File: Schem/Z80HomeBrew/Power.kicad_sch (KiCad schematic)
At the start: 23 parts, among them J1 PJ-037A, Q1 AO3401A, SW1 SW_Push, U1 AMS1117-3.3, U2 LTC2954CTS8-2_TRMPBF

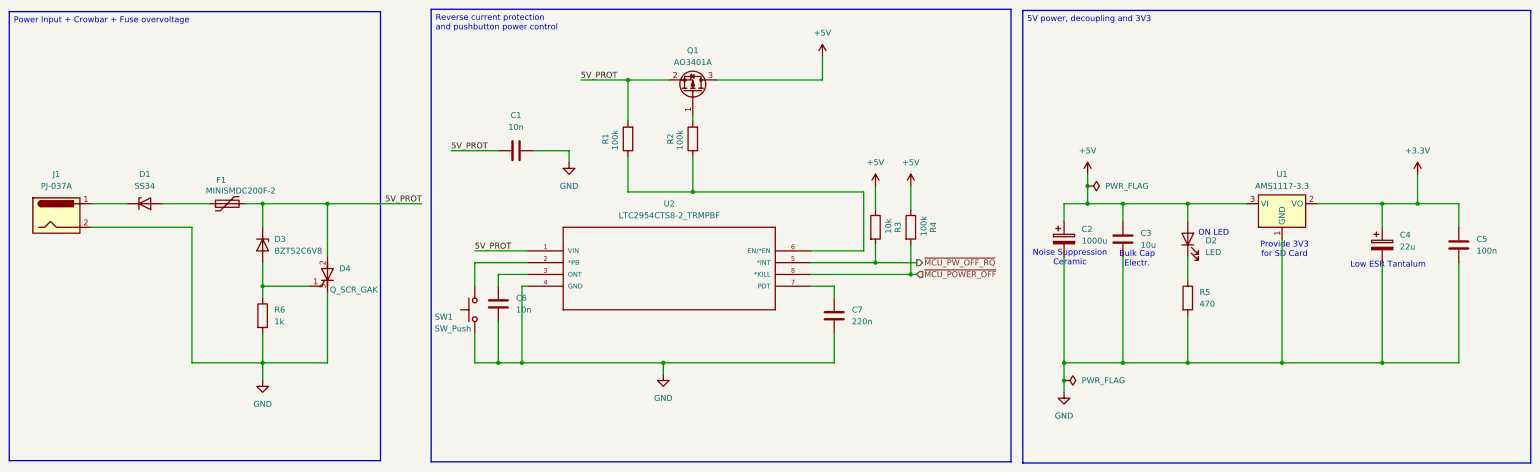
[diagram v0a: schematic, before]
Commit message: Added CPU, Address Decoding, Clock Tree, Console Port, SD Card, USB Ports schematics and associated symbols and footprints.
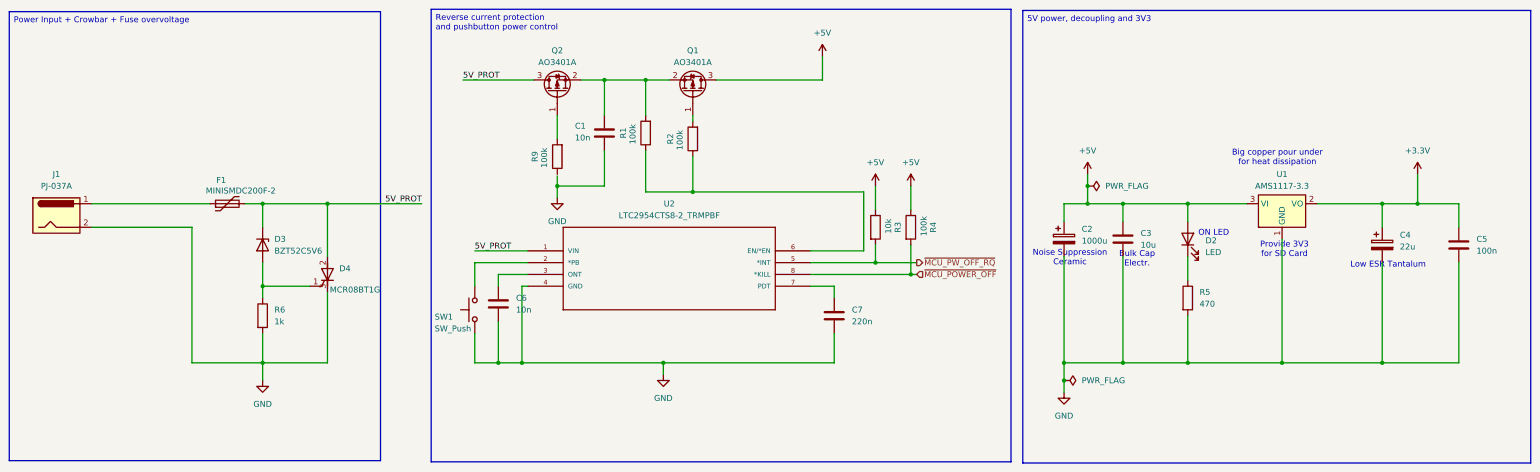
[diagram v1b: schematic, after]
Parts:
- removed D1: SS34, Diode_SMD:D_SMB-SMC_Universal_Handsoldering, symbol Device:D_Zener
- added Q2: AO3401A, Package_TO_SOT_SMD:SOT-23, symbol Transistor_FET:AO3401A
- added R9: 100k, Resistor_SMD:R_0603_1608Metric, symbol Device:R
- D3: value BZT52C6V8 -> BZT52C5V6
- D4: value Q_SCR_GAK -> MCR08BT1G
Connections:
- net 5V_PROT: now also Q2.3 (D); no longer C1.1, Q1.2 (S), R1.2
- net at F1.1: now also J1.1
- new net: C1.1, Q1.2 (S), Q2.2 (S), R1.2
- new net: Q2.1 (G), R9.2
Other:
- note added: "Big copper pour under for heat dissipation"
- moved on the sheet: R1

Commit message: Video block added. fixed some issues with parts...
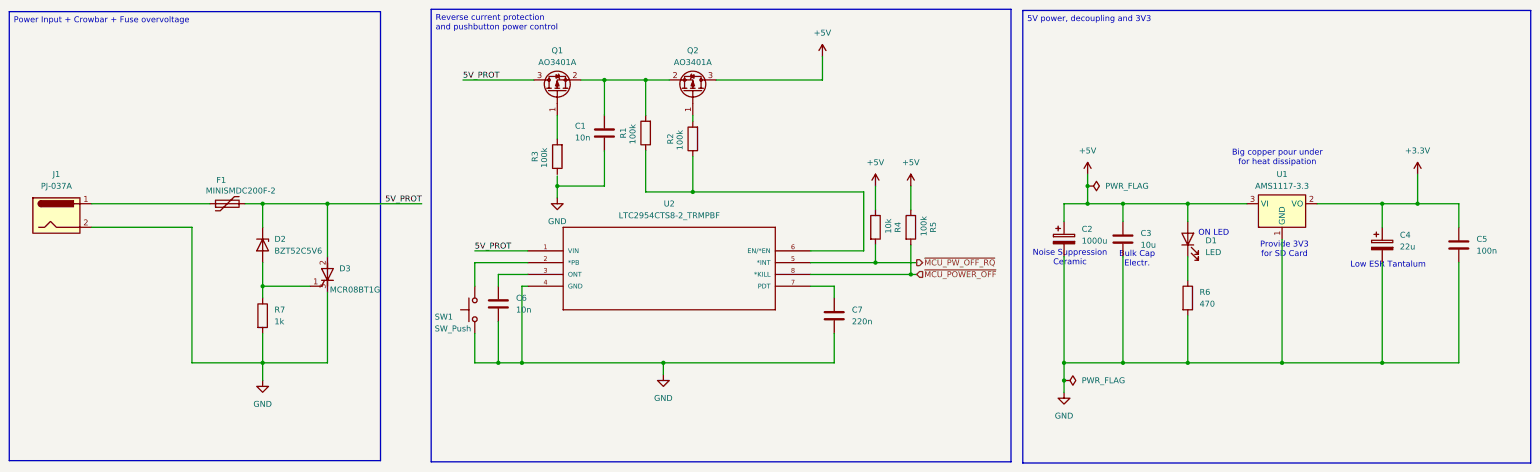
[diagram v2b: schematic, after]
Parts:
- renumbered D2 to D1, D3 to D2, D4 to D3, Q2 to Q1, Q1 to Q2, R9 to R3, R3 to R4, R4 to R5, R5 to R6, R6 to R7
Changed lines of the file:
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@@
 		(on_board yes)
 		(dnp no)
-		(property "Reference" "R4"
+		(property "Reference" "R5"
 			(at 229.616 76.2 90)
 			(effects
@@
 			(project "Z80HomeBrew"
 				(path "/5593e793-d133-45d0-a91e-72805049e474/3988d86f-c93e-49bc-9714-528a8b658c82"
-					(reference "R4")
+					(reference "R5")
 					(unit 1)
 				)
@@
 		(dnp no)
 		(fields_autoplaced yes)
-		(property "Reference" "#PWR05"
+		(property "Reference" "#PWR04"
 			(at 217.17 71.12 0)
 			(effects
@@
 			(project "Z80HomeBrew"
 				(path "/5593e793-d133-45d0-a91e-72805049e474/3988d86f-c93e-49bc-9714-528a8b658c82"
-					(reference "#PWR05")
+					(reference "#PWR04")
 					(unit 1)
 				)
@@
 		(on_board yes)
 		(dnp no)
-		(property "Reference" "R3"
+		(property "Reference" "R4"
 			(at 221.996 76.2 90)
 			(effects
@@
 			(project "Z80HomeBrew"
 				(path "/5593e793-d133-45d0-a91e-72805049e474/3988d86f-c93e-49bc-9714-528a8b658c82"
-					(reference "R3")
+					(reference "R4")
 					(unit 1)
 				)
@@
 		(on_board yes)
 		(dnp no)
-		(property "Reference" "Q2"
+		(property "Reference" "Q1"
 			(at 148.59 38.1 90)
 			(effects
@@
 			(project "Z80HomeBrew"
 				(path "/5593e793-d133-45d0-a91e-72805049e474/3988d86f-c93e-49bc-9714-528a8b658c82"
-					(reference "Q2")
+					(reference "Q1")
 					(unit 1)
 				)
@@
 		(dnp no)
 		(fields_autoplaced yes)
-		(property "Reference" "#PWR03"
+		(property "Reference" "#PWR02"
 			(at 262.89 68.58 0)
 			(effects
@@
 			(project ""
 				(path "/5593e793-d133-45d0-a91e-72805049e474/3988d86f-c93e-49bc-9714-528a8b658c82"
-					(reference "#PWR03")
+					(reference "#PWR02")
 					(unit 1)
 				)
@@
 		(on_board yes)
 		(dnp no)
-		(property "Reference" "R9"
+		(property "Reference" "R3"
 			(at 143.764 60.96 90)
 			(effects
@@
 			(project "Z80HomeBrew"
 				(path "/5593e793-d133-45d0-a91e-72805049e474/3988d86f-c93e-49bc-9714-528a8b658c82"
-					(reference "R9")
+					(reference "R3")
 					(unit 1)
 				)
@@
 		(dnp no)
 		(fields_autoplaced yes)
-		(property "Reference" "R6"
+		(property "Reference" "R7"
 			(at 87.63 93.9799 0)
 			(effects
@@
 			(project "Z80HomeBrew"
 				(path "/5593e793-d133-45d0-a91e-72805049e474/3988d86f-c93e-49bc-9714-528a8b658c82"
-					(reference "R6")
+					(reference "R7")
 					(unit 1)
 				)
@@
 		(dnp no)
 		(fields_autoplaced yes)
-		(property "Reference" "#PWR06"
+		(property "Reference" "#PWR05"
 			(at 224.79 71.12 0)
 			(effects
@@
 			(project "Z80HomeBrew"
 				(path "/5593e793-d133-45d0-a91e-72805049e474/3988d86f-c93e-49bc-9714-528a8b658c82"
-					(reference "#PWR06")
+					(reference "#PWR05")
 					(unit 1)
 				)
@@
 		(on_board yes)
 		(dnp no)
-		(property "Reference" "Q1"
+		(property "Reference" "Q2"
 			(at 177.8 38.1 90)
 			(effects
@@
 			(project ""
 				(path "/5593e793-d133-45d0-a91e-72805049e474/3988d86f-c93e-49bc-9714-528a8b658c82"
-					(reference "Q1")
+					(reference "Q2")
 					(unit 1)
 				)
@@
 		(on_board yes)
 		(dnp no)
-		(property "Reference" "D3"
+		(property "Reference" "D2"
 			(at 87.63 78.7399 90)
 			(effects
@@
 			(project ""
 				(path "/5593e793-d133-45d0-a91e-72805049e474/3988d86f-c93e-49bc-9714-528a8b658c82"
-					(reference "D3")
+					(reference "D2")
 					(unit 1)
 				)
@@
 		(dnp no)
 		(fields_autoplaced yes)
-		(property "Reference" "R5"
+		(property "Reference" "R6"
 			(at 287.02 90.1699 0)
 			(effects
@@
 			(project ""
 				(path "/5593e793-d133-45d0-a91e-72805049e474/3988d86f-c93e-49bc-9714-528a8b658c82"
-					(reference "R5")
+					(reference "R6")
 					(unit 1)
 				)
@@
 		(dnp no)
 		(fields_autoplaced yes)
-		(property "Reference" "#PWR020"
+		(property "Reference" "#PWR06"
 			(at 148.59 76.2 0)
 			(effects
@@
 			(project "Z80HomeBrew"
 				(path "/5593e793-d133-45d0-a91e-72805049e474/3988d86f-c93e-49bc-9714-528a8b658c82"
-					(reference "#PWR020")
+					(reference "#PWR06")
 					(unit 1)
 				)
@@
 		(dnp no)
 		(fields_autoplaced yes)
-		(property "Reference" "#PWR04"
+		(property "Reference" "#PWR03"
 			(at 334.01 68.58 0)
 			(effects
@@
 			(project ""
 				(path "/5593e793-d133-45d0-a91e-72805049e474/3988d86f-c93e-49bc-9714-528a8b658c82"
-					(reference "#PWR04")
+					(reference "#PWR03")
 					(unit 1)
 				)
@@
 		(dnp no)
 		(fields_autoplaced yes)
-		(property "Reference" "D2"
+		(property "Reference" "D1"
 			(at 288.29 79.0574 90)
 			(effects
@@
 			(project ""
 				(path "/5593e793-d133-45d0-a91e-72805049e474/3988d86f-c93e-49bc-9714-528a8b658c82"
-					(reference "D2")
+					(reference "D1")
 					(unit 1)
 				)
@@
 		(on_board yes)
 		(dnp no)
-		(property "Reference" "D4"
+		(property "Reference" "D3"
 			(at 101.6 85.0899 0)
 			(effects
@@
 			(project ""
 				(path "/5593e793-d133-45d0-a91e-72805049e474/3988d86f-c93e-49bc-9714-528a8b658c82"
-					(reference "D4")
-					(unit 1)
-				)
+					(reference "D3")
+					(unit 1)
+				)

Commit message: Completed schematics
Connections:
- net GND: now also R3.1
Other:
- note added: "Replace with 2 pins header for external LED"
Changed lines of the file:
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@@
+		)
+	)
+	(text "Replace with 2 pins\nheader for external LED"
+		(exclude_from_sim no)
+		(at 290.83 85.852 0)
+		(effects
+			(font
+				(size 1.27 1.27)
+			)
 		)
 	)
@@
 	)
 	(junction
-		(at 257.81 109.22)
-		(diameter 0)
-		(color 0 0 0 0)
-	)
-	(junction
 		(at 167.64 44.45)
 		(diameter 0)
@@
 	)
 	(junction
-		(at 262.89 67.31)
-		(diameter 0)
-		(color 0 0 0 0)
-	)
-	(junction
 		(at 284.48 71.12)
 		(diameter 0)
@@
 	(wire
 		(pts
-			(xy 257.81 109.22) (xy 257.81 111.76)
-		)
-		(stroke
-			(width 0)
-			(type default)
-		)
-	)
-	(wire
-		(pts
 			(xy 284.48 105.41) (xy 304.8 105.41)
 		)
@@
 	(wire
 		(pts
-			(xy 262.89 67.31) (xy 262.89 71.12)
+			(xy 262.89 64.77) (xy 262.89 71.12)
 		)
 		(stroke
@@
 	(wire
 		(pts
-			(xy 257.81 105.41) (xy 257.81 109.22)
+			(xy 257.81 105.41) (xy 257.81 111.76)
 		)
 		(stroke
@@
 	(wire
 		(pts
-			(xy 262.89 64.77) (xy 262.89 67.31)
-		)
-		(stroke
-			(width 0)
-			(type default)
-		)
-	)
-	(wire
-		(pts
 			(xy 214.63 81.28) (xy 203.2 81.28)
 		)
@@
 	(wire
 		(pts
-			(xy 148.59 65.135) (xy 148.59 67.31)
+			(xy 148.59 64.77) (xy 148.59 67.31)
 		)
 		(stroke
@@
 	)
 	(symbol
-		(lib_id "power:PWR_FLAG")
-		(at 262.89 67.31 270)
-		(unit 1)
-		(exclude_from_sim no)
-		(in_bom yes)
-		(on_board yes)
-		(dnp no)
-		(fields_autoplaced yes)
-		(property "Reference" "#FLG01"
-			(at 264.795 67.31 0)
-			(effects
-				(font
-					(size 1.27 1.27)
-				)
-				(hide yes)
-			)
-		)
-		(property "Value" "PWR_FLAG"
-			(at 266.7 67.3099 90)
-			(effects
-				(font
-					(size 1.27 1.27)
-				)
-				(justify left)
-			)
-		)
-		(property "Footprint" ""
-			(at 262.89 67.31 0)
-			(effects
-				(font
-					(size 1.27 1.27)
-				)
-				(hide yes)
-			)
-		)
-		(property "Datasheet" "~"
-			(at 262.89 67.31 0)
-			(effects
-				(font
-					(size 1.27 1.27)
-				)
-				(hide yes)
-			)
-		)
-		(property "Description" "Special symbol for telling ERC where power comes from"
-			(at 262.89 67.31 0)
-			(effects
-				(font
-					(size 1.27 1.27)
-				)
-				(hide yes)
-			)
-		)
-		(pin "1"
-		)
-		(instances
-			(project ""
-				(path "/5593e793-d133-45d0-a91e-72805049e474/3988d86f-c93e-49bc-9714-528a8b658c82"
-					(reference "#FLG01")
-					(unit 1)
-				)
-			)
-			(project "Power"
-				(path "/b434dbaa-625e-4b8b-b58d-a44d69f34612"
-					(reference "#FLG01")
-					(unit 1)
-				)
-			)
-		)
-	)
-	(symbol
 		(lib_id "power:+5V")
 		(at 217.17 67.31 0)
@@
 					(unit 1)
 				)
-			)
-		)
-	)
-	(symbol
-		(lib_id "power:PWR_FLAG")
-		(at 257.81 109.22 270)
-		(unit 1)
-		(exclude_from_sim no)
-		(in_bom yes)
-		(on_board yes)
-		(dnp no)
-		(fields_autoplaced yes)
-		(property "Reference" "#FLG02"
-			(at 259.715 109.22 0)
-			(effects
-				(font
-					(size 1.27 1.27)
-				)
-				(hide yes)
-			)
-		)
-		(property "Value" "PWR_FLAG"
-			(at 261.62 109.2199 90)
-			(effects
-				(font
-					(size 1.27 1.27)
-				)
-				(justify left)
-			)
-		)
-		(property "Footprint" ""
-			(at 257.81 109.22 0)
-			(effects
-				(font
-					(size 1.27 1.27)
-				)
-				(hide yes)
-			)
-		)
-		(property "Datasheet" "~"
-			(at 257.81 109.22 0)
-			(effects
-				(font
-					(size 1.27 1.27)
-				)
-				(hide yes)
-			)
-		)
-		(property "Description" "Special symbol for telling ERC where power comes from"
-			(at 257.81 109.22 0)
-			(effects
-				(font
-					(size 1.27 1.27)
-				)
-				(hide yes)
-			)
-		)
-		(pin "1"
-		)
-		(instances
-			(project ""
-				(path "/5593e793-d133-45d0-a91e-72805049e474/3988d86f-c93e-49bc-9714-528a8b658c82"
-					(reference "#FLG02")
-					(unit 1)
-				)
-			)
-			(project "Power"
-				(path "/b434dbaa-625e-4b8b-b58d-a44d69f34612"
-					(reference "#FLG02")
-					(unit 1)
-				)

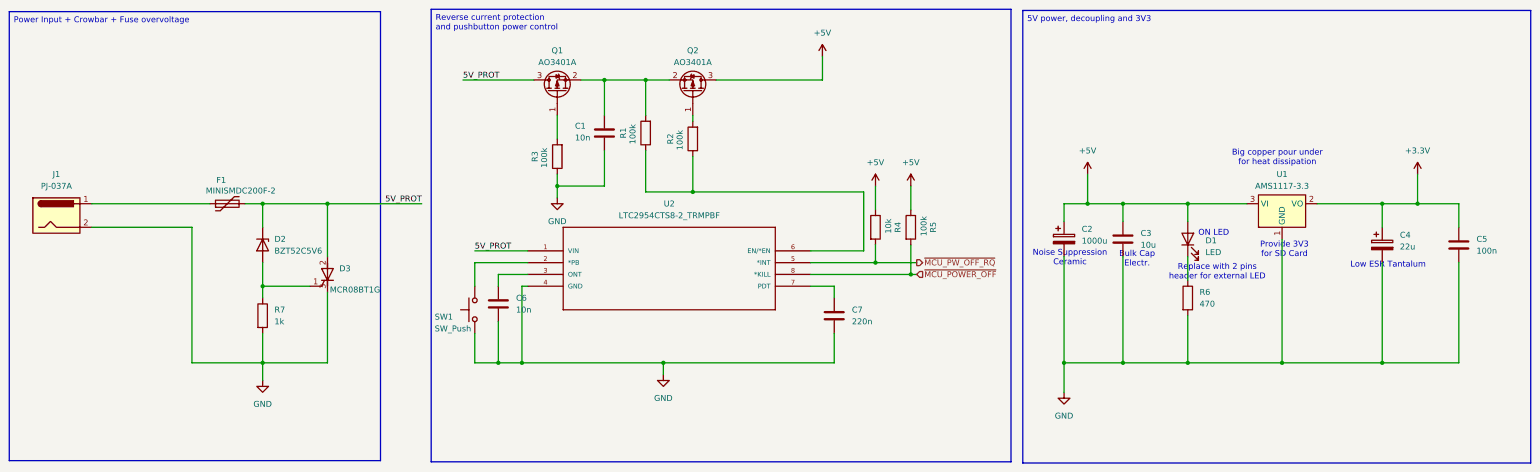
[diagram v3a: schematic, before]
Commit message: Added pBITzBackplane and MezzanineConnector
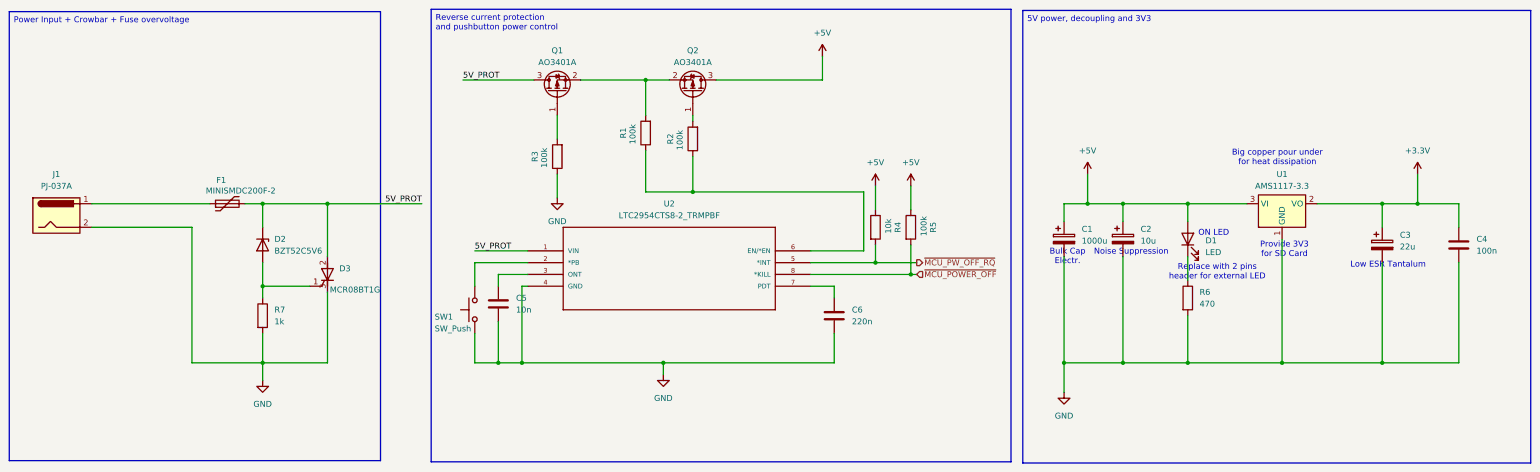
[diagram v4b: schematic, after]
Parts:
- removed C1: 10n, Capacitor_SMD:C_0805_2012Metric, symbol Device:C
- removed C3: 10u, Capacitor_SMD:C_0805_2012Metric, symbol Device:C
- added C2: 10u, Capacitor_THT:CP_Radial_D5.0mm_P2.50mm, symbol Device:C_Polarized
- C1: renamed from C2; footprint Capacitor_SMD:CP_Elec_10x10.5 -> Capacitor_THT:CP_Radial_D10.0mm_P5.00mm; MANUFACTURER_PART_NUMBER (none) -> 16YXJ1000MT810X16
- C3: renamed from C4; MANUFACTURER_PART_NUMBER (none) -> T494B226M016AT
- C4: renamed from C5; MANUFACTURER_PART_NUMBER (none) -> 0402B104K160CT
- C5: renamed from C6; footprint Capacitor_SMD:C_0805_2012Metric -> Capacitor_SMD:C_0603_1608Metric; MANUFACTURER_PART_NUMBER (none) -> C0603C103K4RACTU
- C6: renamed from C7; footprint Capacitor_SMD:C_0805_2012Metric -> Capacitor_SMD:C_0603_1608Metric; MANUFACTURER_PART_NUMBER (none) -> CL05B224KO5NNNC
- D1: MANUFACTURER_PART_NUMBER (none) -> LTST-C150GKT
- D2: MANUFACTURER_PART_NUMBER (none) -> BZT52C5V6
- D3: MANUFACTURER_PART_NUMBER (none) -> MCR08BT1G
- F1: MANUFACTURER_PART_NUMBER (none) -> MINISMDC200F-2
- J1: MANUFACTURER_PART_NUMBER (none) -> PJ-037A
- Q1, Q2: MANUFACTURER_PART_NUMBER (none) -> AO3401A
- R1, R2, R3, R5: MANUFACTURER_PART_NUMBER (none) -> RMCF0603FT100K
- R4: MANUFACTURER_PART_NUMBER (none) -> RC0603FR-0710KL
- R6: MANUFACTURER_PART_NUMBER (none) -> RC0603JR-07470RL
- R7: MANUFACTURER_PART_NUMBER (none) -> RMCF0603FT1K00
- U1: MANUFACTURER_PART_NUMBER (none) -> AMS1117-3.3
- U2: MANUFACTURER_PART_NUMBER ltc2954cts81 -> LTC2954CTS8-1#TRMBF
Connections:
- net +5V: now also C2.1
- net GND: now also C2.2
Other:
- note added: "Noise Suppression"
- note removed: "Noise Suppression Ceramic"
